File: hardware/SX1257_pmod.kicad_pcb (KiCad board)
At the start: 4 copper layers, 20.3 x 45.5 mm, 47 parts, among them J1 Conn_02x06_Odd_Even, J2 SMA_F_RX, J3 SMA_F_TX, U1 SX1257, U2 SC18IS602B, Y1 36MHz 10ppm

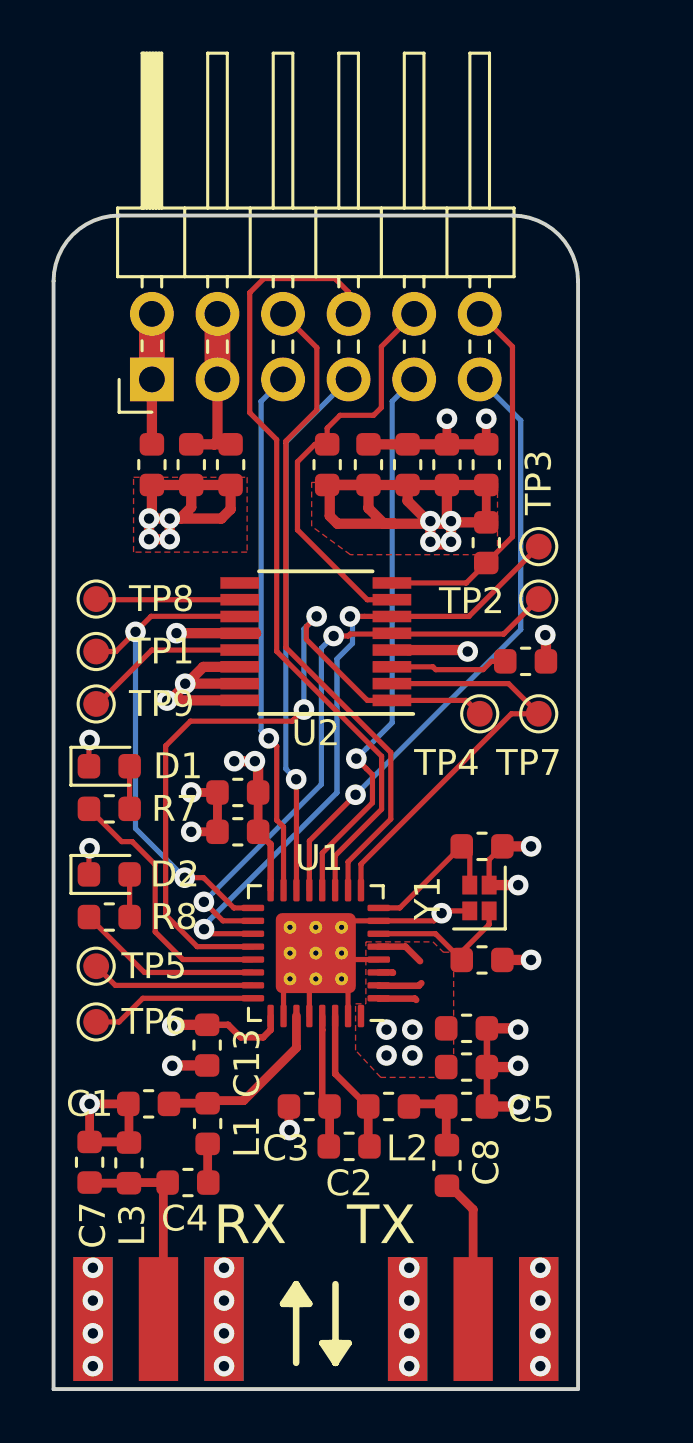
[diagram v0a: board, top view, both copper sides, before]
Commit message: Fix VR_* pins & change most passives to 0402
This fixes the power pin wiring as mentioned in the RevB errata:
SX1257 VR_* pins are now only connected to decoupling caps.

This also moves a lot of caps away from the PMOD header & closer to
the appropriate power pins.

Space was getting tight, so this also changes small caps & inductors
to 0402. As a result, there's also a bit of re-routing to reconnect things.
The RF paths should flow a bit better now.
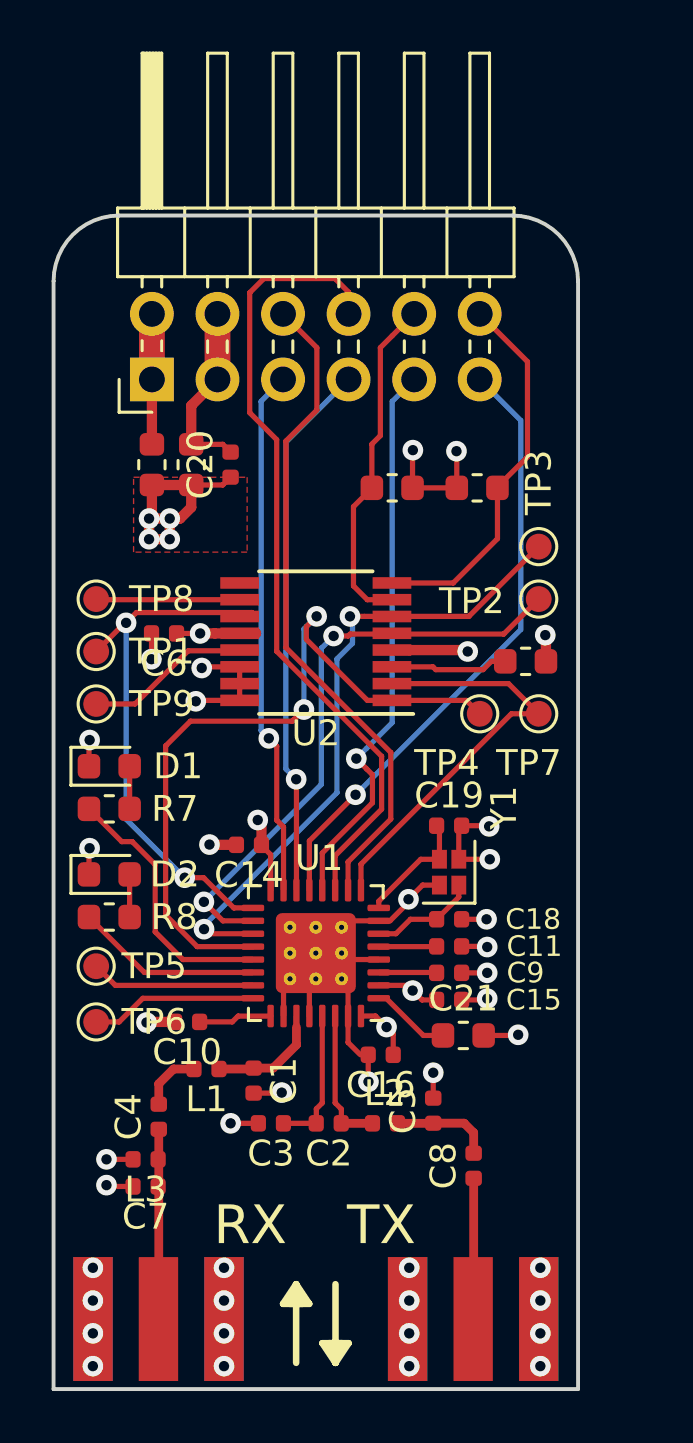
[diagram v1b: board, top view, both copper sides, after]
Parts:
- removed C12, C13: 10n, Capacitor_SMD:C_0603_1608Metric
- added C21: 10u, Capacitor_SMD:C_0603_1608Metric, F.Cu at (130.2, 54.6)
- C1, C10, C11, C14, C15, C16, C18, C19, C2, C20, C3, C4, C5, C6, C7, C8, C9: footprint Capacitor_SMD:C_0603_1608Metric -> Capacitor_SMD:C_0402_1005Metric
- L1, L2, L3: footprint Inductor_SMD:L_0603_1608Metric -> Inductor_SMD:L_0402_1005Metric
- moved C16 22.9 mm to (127.0, 55.4), turned to 180 degrees
- moved C15 20.7 mm to (129.6, 53.2), turned to 0 degrees
- moved C9 19.9 mm to (129.6, 52.2), turned to 0 degrees
- moved C14 17.4 mm to (121.9, 47.2), turned to 180 degrees
- moved C10 11.0 mm to (119.5, 54.1), turned to 180 degrees
- moved C6 6.79 mm to (118.6, 39.0)
- moved C1 4.17 mm to (122.0, 56.4), turned to 270 degrees
- moved C11 3.25 mm to (129.6, 51.2)
- moved C4 2.79 mm to (118.4, 57.8), turned to 90 degrees
- moved R2 2.68 mm to (127.4, 33.4), turned to 180 degrees
- moved C7 2.36 mm to (117.9, 60.5), turned to 180 degrees
- moved R1 2.15 mm to (130.7, 33.4), turned to 0 degrees
- moved L1 2.11 mm to (120.2, 55.9), turned to 180 degrees
- moved C18 2.03 mm to (129.6, 50.1)
- moved C3 1.62 mm to (122.7, 58.0)
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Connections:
- C10 pad 1: +3V3 -> /VR_ANA2
- C11 pad 1: +3V3 -> /VR_DIG
- C9 pad 1: +3V3 -> /VR_ANA1
- U1 pad 1: +3V3 -> /VR_PA
- U1 pad 25: +3V3 -> /VR_ANA2
- U1 pad 3: +3V3 -> /VR_ANA1
- U1 pad 5: +3V3 -> /VR_DIG
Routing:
- net +3V3: track 58.0 -> 26.1 mm, vias 17 -> 11
- net GND: track 82.5 -> 65.5 mm, vias 35 -> 38
- net /I2C_SDA: track 17.1 -> 13.2 mm
- net /VR_PA: track 0.00 -> 3.09 mm
- net /VR_ANA2: track 0.00 -> 2.84 mm
- net /RF_IN: track 7.07 -> 4.50 mm
- net /VR_ANA1: track 0.00 -> 2.25 mm
- net /VR_DIG: track 0.00 -> 2.25 mm
- net /XTA: track 5.98 -> 4.16 mm
- net /XTB: track 5.83 -> 4.63 mm
- net Net-(C5-Pad1): track 2.96 -> 3.90 mm
- net Net-(C4-Pad2): track 1.51 -> 2.39 mm
- net Net-(C4-Pad1): track 8.22 -> 7.36 mm
- net /I2C_SCL: track 13.9 -> 14.8 mm
- net /SPI_SCK: track 20.2 -> 20.8 mm

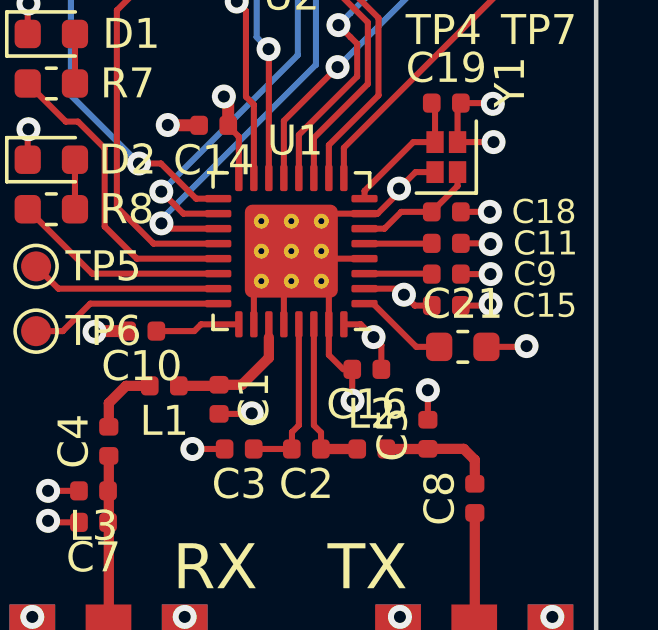
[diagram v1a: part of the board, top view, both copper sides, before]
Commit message: Change C21 (VR_PA) to 10n
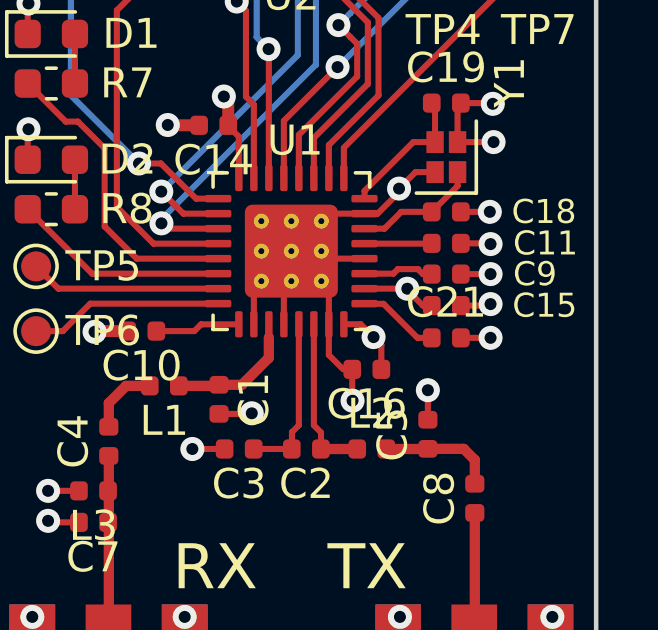
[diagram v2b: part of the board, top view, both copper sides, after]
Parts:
- C21: value 10u -> 10n; footprint Capacitor_SMD:C_0603_1608Metric -> Capacitor_SMD:C_0402_1005Metric
- moved C21 0.63 mm to (129.6, 54.3)
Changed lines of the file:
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@@
     (thickness 1.6)
     (drawings 60)
-    (tracks 361)
+    (tracks 365)
     (zones 0)
     (modules 46)
@@
     (add_net "Net-(R9-Pad2)")
   )
+  (module Capacitor_SMD:C_0402_1005Metric (layer F.Cu)
+    (at 129.625 54.325)
+    (descr "Capacitor SMD 0402 (1005 Metric), square (rectangular) end terminal, IPC_7351 nominal, (Body size source: http://www.tortai-tech.com/upload/download/2011102023233369053.pdf), generated with kicad-footprint-generator")
+    (tags capacitor)
+    (attr smd)
+    (fp_text reference C21 (at 0 -1.17) (layer F.SilkS)
+      (effects (font (size 1 1) (thickness 0.15)))
+    )
+    (fp_text value 10n (at 0 1.17) (layer F.Fab)
+      (effects (font (size 1 1) (thickness 0.15)))
+    )
+    (fp_text user %R (at 0 0) (layer F.Fab)
+      (effects (font (size 0.25 0.25) (thickness 0.04)))
+    )
+    (fp_line (start 0.93 0.47) (end -0.93 0.47) (layer F.CrtYd) (width 0.05))
+    (fp_line (start 0.93 -0.47) (end 0.93 0.47) (layer F.CrtYd) (width 0.05))
+    (fp_line (start -0.93 -0.47) (end 0.93 -0.47) (layer F.CrtYd) (width 0.05))
+    (fp_line (start -0.93 0.47) (end -0.93 -0.47) (layer F.CrtYd) (width 0.05))
+    (fp_line (start 0.5 0.25) (end -0.5 0.25) (layer F.Fab) (width 0.1))
+    (fp_line (start 0.5 -0.25) (end 0.5 0.25) (layer F.Fab) (width 0.1))
+    (fp_line (start -0.5 -0.25) (end 0.5 -0.25) (layer F.Fab) (width 0.1))
+    (fp_line (start -0.5 0.25) (end -0.5 -0.25) (layer F.Fab) (width 0.1))
+    (pad 2 smd roundrect (at 0.485 0) (size 0.59 0.64) (layers F.Cu F.Paste F.Mask) (roundrect_rratio 0.25)
+      (net 1 GND))
+    (pad 1 smd roundrect (at -0.485 0) (size 0.59 0.64) (layers F.Cu F.Paste F.Mask) (roundrect_rratio 0.25)
+      (net 39 /VR_PA))
+    (model ${KISYS3DMOD}/Capacitor_SMD.3dshapes/C_0402_1005Metric.wrl
+      (at (xyz 0 0 0))
+      (scale (xyz 1 1 1))
+      (rotate (xyz 0 0 0))
+    )
+  )
   (module Inductor_SMD:L_0402_1005Metric (layer F.Cu)
     (at 117.865 59.425 180)
@@
     )
   )
-  (module Capacitor_SMD:C_0603_1608Metric (layer F.Cu)
-    (at 130.175 54.625)
-    (descr "Capacitor SMD 0603 (1608 Metric), square (rectangular) end terminal, IPC_7351 nominal, (Body size source: http://www.tortai-tech.com/upload/download/2011102023233369053.pdf), generated with kicad-footprint-generator")
-    (tags capacitor)
-    (attr smd)
-    (fp_text reference C21 (at 0 -1.43) (layer F.SilkS)
-      (effects (font (size 1 1) (thickness 0.15)))
-    )
-    (fp_text value 10u (at 0 1.43) (layer F.Fab)
-      (effects (font (size 1 1) (thickness 0.15)))
-    )
-    (fp_text user %R (at 0 0) (layer F.Fab)
-      (effects (font (size 0.4 0.4) (thickness 0.06)))
-    )
-    (fp_line (start 1.48 0.73) (end -1.48 0.73) (layer F.CrtYd) (width 0.05))
-    (fp_line (start 1.48 -0.73) (end 1.48 0.73) (layer F.CrtYd) (width 0.05))
-    (fp_line (start -1.48 -0.73) (end 1.48 -0.73) (layer F.CrtYd) (width 0.05))
-    (fp_line (start -1.48 0.73) (end -1.48 -0.73) (layer F.CrtYd) (width 0.05))
-    (fp_line (start -0.162779 0.51) (end 0.162779 0.51) (layer F.SilkS) (width 0.12))
-    (fp_line (start -0.162779 -0.51) (end 0.162779 -0.51) (layer F.SilkS) (width 0.12))
-    (fp_line (start 0.8 0.4) (end -0.8 0.4) (layer F.Fab) (width 0.1))
-    (fp_line (start 0.8 -0.4) (end 0.8 0.4) (layer F.Fab) (width 0.1))
-    (fp_line (start -0.8 -0.4) (end 0.8 -0.4) (layer F.Fab) (width 0.1))
-    (fp_line (start -0.8 0.4) (end -0.8 -0.4) (layer F.Fab) (width 0.1))
-    (pad 2 smd roundrect (at 0.7875 0) (size 0.875 0.95) (layers F.Cu F.Paste F.Mask) (roundrect_rratio 0.25)
-      (net 1 GND))
-    (pad 1 smd roundrect (at -0.7875 0) (size 0.875 0.95) (layers F.Cu F.Paste F.Mask) (roundrect_rratio 0.25)
-      (net 39 /VR_PA))
-    (model ${KISYS3DMOD}/Capacitor_SMD.3dshapes/C_0603_1608Metric.wrl
-      (at (xyz 0 0 0))
-      (scale (xyz 1 1 1))
-      (rotate (xyz 0 0 0))
-    )
-  )
   (module extra:Crystal_SMD_1612-4Pin_1.6x1.2mm (layer F.Cu)
     (at 129.625 48.3 90)
@@
   (segment (start 130.11 53.25) (end 131.05 53.25) (width 0.2032) (layer F.Cu) (net 1))
   (segment (start 131.05 53.25) (end 131.1 53.2) (width 0.2032) (layer F.Cu) (net 1))
-  (via (at 132.3 54.6) (size 0.8) (drill 0.4) (layers F.Cu B.Cu) (net 1))
-  (segment (start 130.9625 54.625) (end 132.275 54.625) (width 0.2032) (layer F.Cu) (net 1))
-  (segment (start 132.275 54.625) (end 132.3 54.6) (width 0.2032) (layer F.Cu) (net 1))
   (segment (start 130 46.61) (end 130.11 46.5) (width 0.2032) (layer F.Cu) (net 1))
   (segment (start 130 47.8) (end 130 46.61) (width 0.2032) (layer F.Cu) (net 1))
@@
   (segment (start 119.634 30.226) (end 120.65 29.21) (width 0.4) (layer F.Cu) (net 1))
   (segment (start 119.634 31.7245) (end 119.634 30.226) (width 0.4) (layer F.Cu) (net 1))
+  (via (at 131.1 54.325) (size 0.8) (drill 0.4) (layers F.Cu B.Cu) (net 1))
+  (segment (start 130.11 54.325) (end 131.1 54.325) (width 0.2032) (layer F.Cu) (net 1))
   (segment (start 126.8975 50.685) (end 127.565 50.685) (width 0.2032) (layer F.Cu) (net 2))
   (segment (start 128.125 50.125) (end 129.14 50.125) (width 0.2032) (layer F.Cu) (net 2))
@@
   (segment (start 133.3755 40.132) (end 133.3755 39.1415) (width 0.4) (layer F.Cu) (net 6) (status 10))
   (segment (start 133.3755 39.1415) (end 133.35 39.116) (width 0.2032) (layer F.Cu) (net 6))
-  (segment (start 128.575 53.25) (end 129.14 53.25) (width 0.2032) (layer F.Cu) (net 6))
-  (segment (start 126.8975 52.685) (end 128.01 52.685) (width 0.2032) (layer F.Cu) (net 6))
-  (segment (start 128.01 52.685) (end 128.2125 52.8875) (width 0.2032) (layer F.Cu) (net 6))
   (via (at 127.2 54.3) (size 0.8) (drill 0.4) (layers F.Cu B.Cu) (net 6))
   (segment (start 127.46 55.375) (end 127.46 54.56) (width 0.2032) (layer F.Cu) (net 6))
@@
   (segment (start 126.7725 53.8725) (end 126.21 53.8725) (width 0.2032) (layer F.Cu) (net 6))
   (segment (start 127.2 54.3) (end 126.7725 53.8725) (width 0.2032) (layer F.Cu) (net 6))
-  (segment (start 128.2125 52.8875) (end 128.575 53.25) (width 0.2032) (layer F.Cu) (net 6))
-  (via (at 128.2125 52.8875) (size 0.8) (drill 0.4) (layers F.Cu B.Cu) (net 6))
   (segment (start 122.71 47.62) (end 122.71 48.9975) (width 0.2032) (layer F.Cu) (net 6))
   (segment (start 122.355 47.24) (end 122.355 47.265) (width 0.2032) (layer F.Cu) (net 6))
@@
   (segment (start 119.634 33.2995) (end 119.634 34.166) (width 0.4) (layer F.Cu) (net 6) (status 10))
   (segment (start 119.2 34.6) (end 118.8 34.6) (width 0.4) (layer F.Cu) (net 6))
+  (segment (start 128.322758 52.685) (end 128.325116 52.687358) (width 0.2032) (layer F.Cu) (net 6))
+  (segment (start 129.14 53.25) (end 128.845 53.25) (width 0.2032) (layer F.Cu) (net 6))
+  (segment (start 128.845 53.25) (end 128.325116 52.730116) (width 0.2032) (layer F.Cu) (net 6))
+  (segment (start 126.8975 52.685) (end 128.322758 52.685) (width 0.2032) (layer F.Cu) (net 6))
+  (via (at 128.325116 52.687358) (size 0.8) (drill 0.4) (layers F.Cu B.Cu) (net 6))
+  (segment (start 128.325116 52.730116) (end 128.325116 52.687358) (width 0.2032) (layer F.Cu) (net 6))
   (segment (start 117.8185 52.185) (end 115.6715 50.038) (width 0.2032) (layer F.Cu) (net 7) (status 20))
   (segment (start 122.0225 52.185) (end 117.8185 52.185) (width 0.2032) (layer F.Cu) (net 7) (status 10))
@@
   (segment (start 131.4975 33.41) (end 131.4975 33.3725) (width 0.2032) (layer F.Cu) (net 35))
   (segment (start 131.4975 33.3725) (end 132.66 32.21) (width 0.2032) (layer F.Cu) (net 35))
-  (segment (start 129.125 52.185) (end 129.14 52.2) (width 0.2032) (layer F.Cu) (net 36))
-  (segment (start 126.8975 52.185) (end 129.125 52.185) (width 0.2032) (layer F.Cu) (net 36))
+  (segment (start 128.011194 52.033356) (end 128.678356 52.033356) (width 0.2032) (layer F.Cu) (net 36))
+  (segment (start 128.678356 52.033356) (end 128.845 52.2) (width 0.2032) (layer F.Cu) (net 36))
+  (segment (start 128.845 52.2) (end 129.14 52.2) (width 0.2032) (layer F.Cu) (net 36))
+  (segment (start 127.85955 52.185) (end 128.011194 52.033356) (width 0.2032) (layer F.Cu) (net 36))
+  (segment (start 126.8975 52.185) (end 127.85955 52.185) (width 0.2032) (layer F.Cu) (net 36))
   (segment (start 122.7075 53.875) (end 122.71 53.8725) (width 0.2032) (layer F.Cu) (net 37))
   (segment (start 121.45 53.875) (end 122.7075 53.875) (width 0.2032) (layer F.Cu) (net 37))
@@
   (segment (start 129.13 51.185) (end 129.14 51.175) (width 0.2032) (layer F.Cu) (net 38))
   (segment (start 126.8975 51.185) (end 129.13 51.185) (width 0.2032) (layer F.Cu) (net 38))
-  (segment (start 128.625 54.625) (end 129.3875 54.625) (width 0.2032) (layer F.Cu) (net 39))
-  (segment (start 126.8975 53.185) (end 127.185 53.185) (width 0.2032) (layer F.Cu) (net 39))
-  (segment (start 127.185 53.185) (end 128.625 54.625) (width 0.2032) (layer F.Cu) (net 39))
+  (segment (start 128.665 54.325) (end 129.14 54.325) (width 0.2032) (layer F.Cu) (net 39))
+  (segment (start 127.53 53.19) (end 128.665 54.325) (width 0.2032) (layer F.Cu) (net 39))
+  (segment (start 126.8975 53.185) (end 126.9025 53.19) (width 0.2032) (layer F.Cu) (net 39))
+  (segment (start 126.9025 53.19) (end 127.53 53.19) (width 0.2032) (layer F.Cu) (net 39))
   (zone (net 1) (net_name GND) (layer In1.Cu) (hatch edge 0.508)
     (connect_pads (clearance 0.508))
